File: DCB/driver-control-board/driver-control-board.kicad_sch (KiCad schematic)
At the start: 34 parts, among them U1 STM32F413CGUx, U2 LD1117S33TR_SOT223

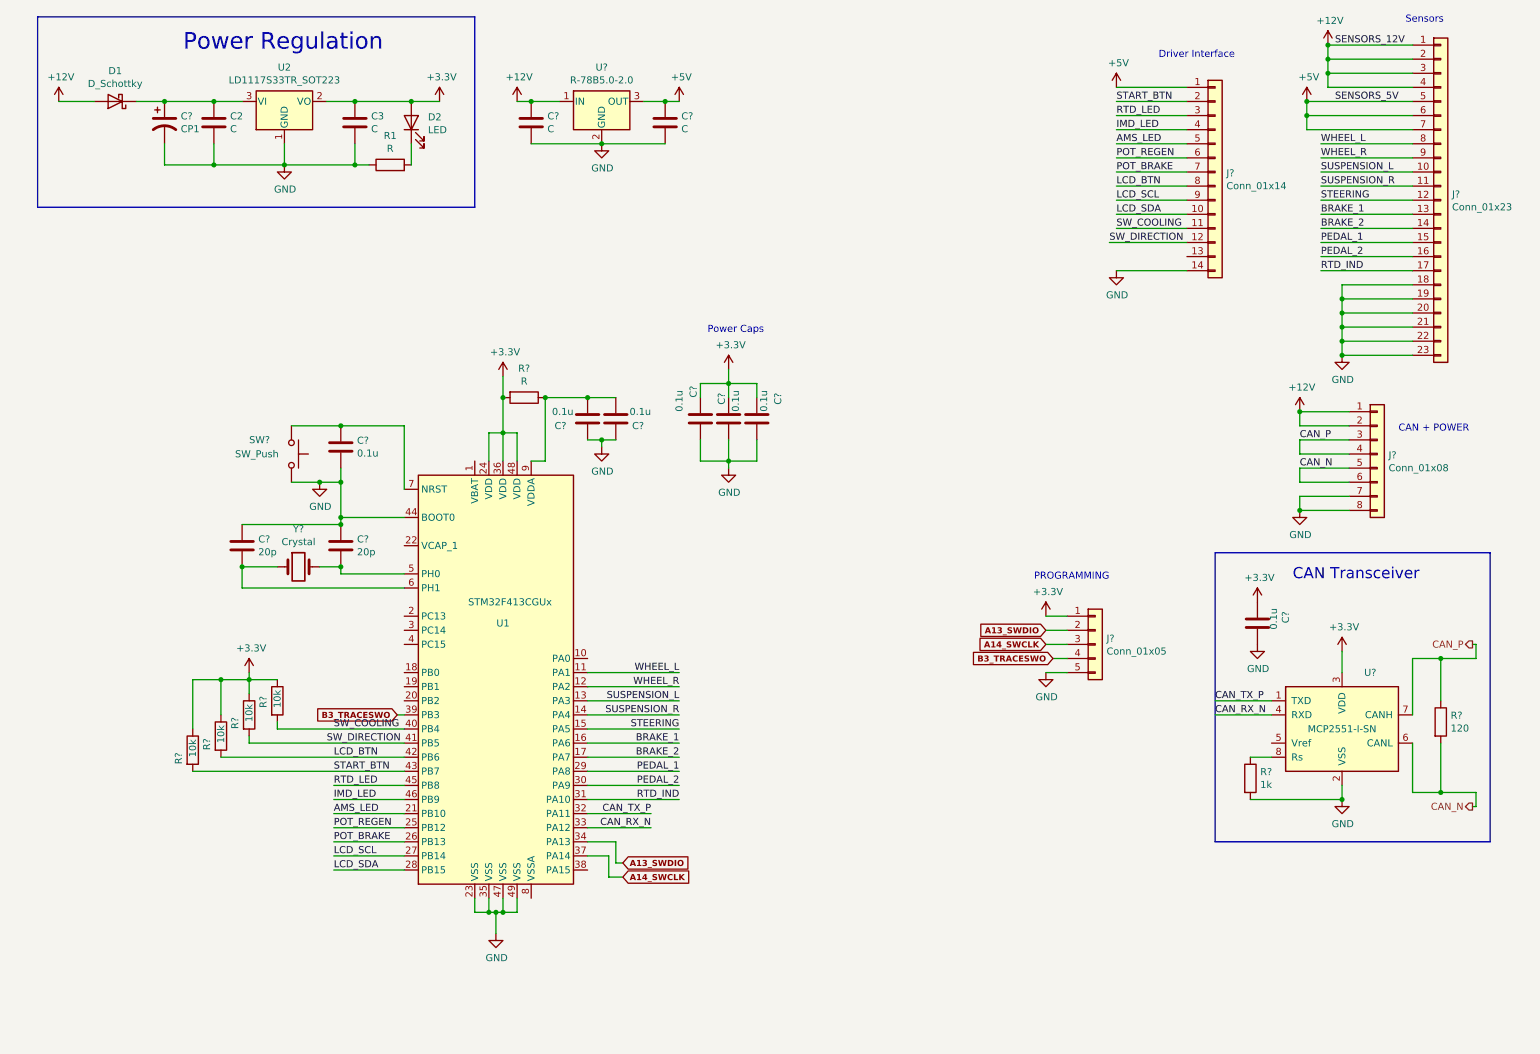
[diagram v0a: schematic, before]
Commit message: DCB Layout Rev 1 Complete
Complete the layout first draft
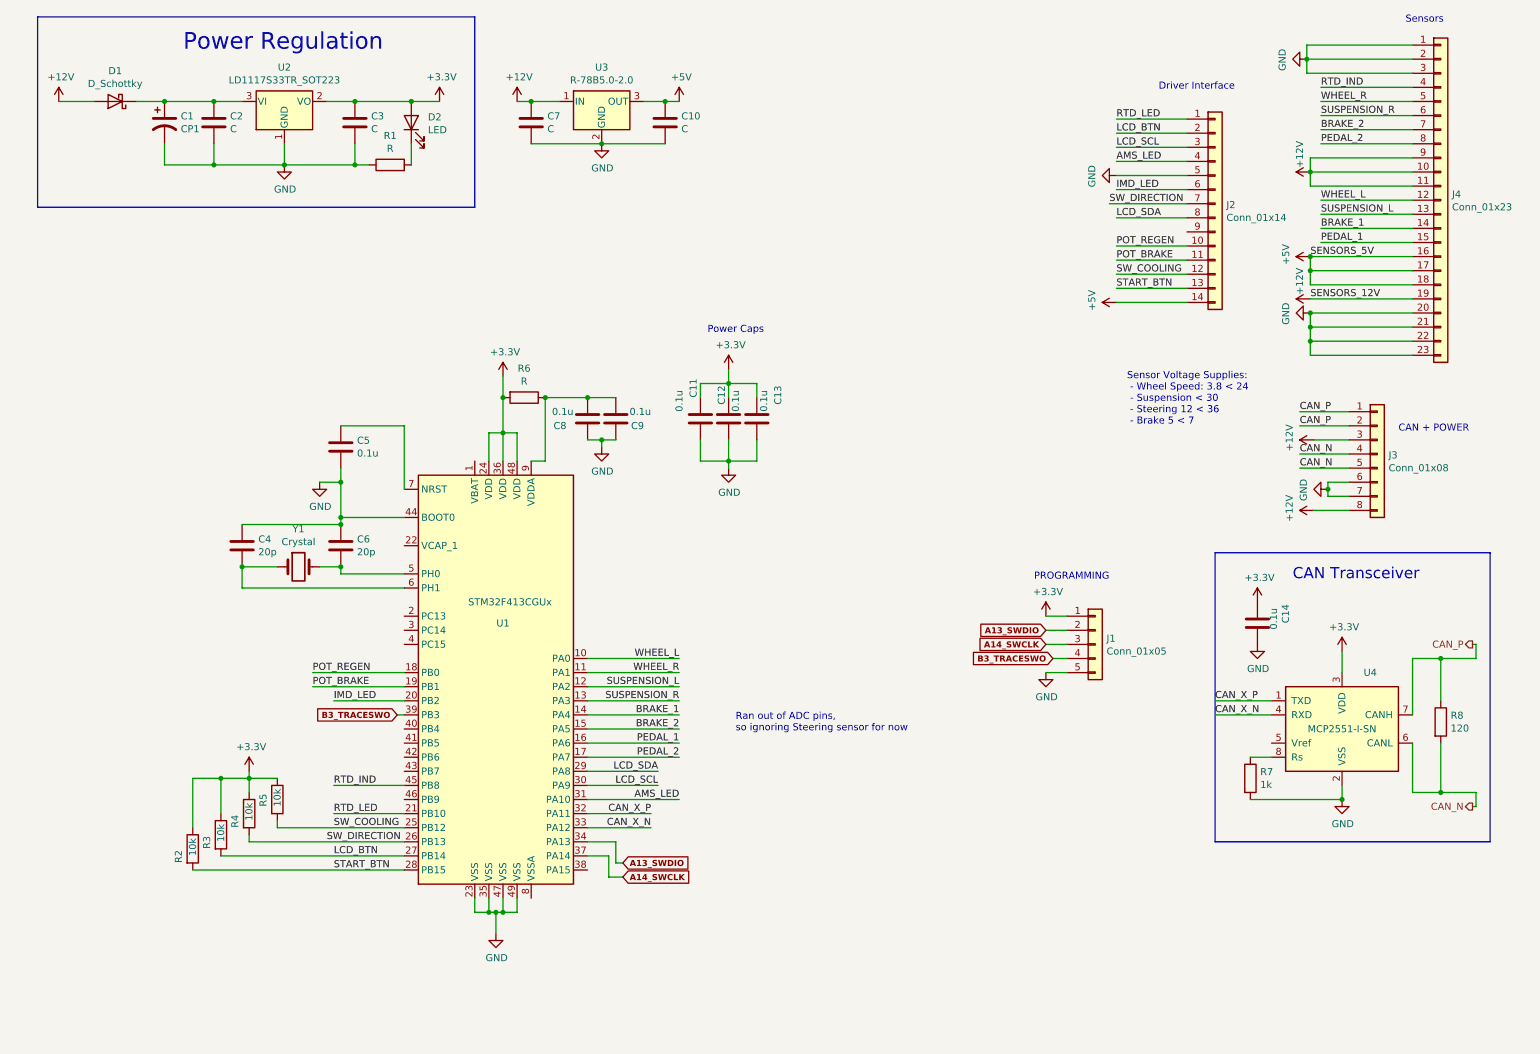
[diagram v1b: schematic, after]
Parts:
- removed SW?: SW_Push, symbol Switch:SW_Push
- C1: renamed from C?; footprint (none) -> Capacitor_THT:CP_Radial_D4.0mm_P2.00mm
- C10, C11, C12, C13, C14, C4, C5, C6, C7, C8, C9: renamed from C?; footprint (none) -> Capacitor_SMD:C_0603_1608Metric_Pad1.08x0.95mm_HandSolder
- C2, C3: footprint (none) -> Capacitor_SMD:C_0603_1608Metric_Pad1.08x0.95mm_HandSolder
- D1: footprint (none) -> Diode_SMD:D_SMA-SMB_Universal_Handsoldering
- D2: footprint (none) -> LED_SMD:LED_0603_1608Metric_Pad1.05x0.95mm_HandSolder
- J1: renamed from J?; footprint (none) -> Connector_JST:JST_XH_B5B-XH-A_1x05_P2.50mm_Vertical
- J2: renamed from J?; footprint (none) -> AERO_Footprints:TE_1-776266-1_14pin_Horizontal
- J3: renamed from J?; footprint (none) -> AERO_Footprints:TE_1-776280-1_8pin_Horizontal
- J4: renamed from J?; footprint (none) -> AERO_Footprints:TE_1-770669-1_23pin_Horizontal
- R1: footprint (none) -> Resistor_SMD:R_0603_1608Metric_Pad0.98x0.95mm_HandSolder
- R2, R3, R4, R5, R6, R7, R8: renamed from R?; footprint (none) -> Resistor_SMD:R_0603_1608Metric_Pad0.98x0.95mm_HandSolder
- Y1: renamed from Y?; footprint (none) -> Crystal:Crystal_HC52-8mm_Vertical
- gave numbers to parts that had none: 2
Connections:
- net +12V: now also J3.3 (Pin_3), J3.8 (Pin_8), J4.10 (Pin_10), J4.11 (Pin_11), J4.19 (Pin_19), J4.9 (Pin_9); no longer J3.1 (Pin_1), J3.2 (Pin_2), J4.1 (Pin_1), J4.2 (Pin_2), J4.3 (Pin_3), J4.4 (Pin_4)
- net +5V: now also J2.14 (Pin_14), J4.16 (Pin_16), J4.17 (Pin_17), J4.18 (Pin_18); no longer J2.1 (Pin_1), J4.5 (Pin_5), J4.6 (Pin_6), J4.7 (Pin_7)
- net AMS_LED: now also J2.4 (Pin_4), U1.31 (PA10); no longer J2.5 (Pin_5), U1.21 (PB10)
- net BRAKE_1: now also J4.14 (Pin_14), U1.14 (PA4); no longer J4.13 (Pin_13), U1.16 (PA6)
- net BRAKE_2: now also J4.7 (Pin_7), U1.15 (PA5); no longer J4.14 (Pin_14), U1.17 (PA7)
- net CAN_N: now also J3.4 (Pin_4); no longer J3.6 (Pin_6)
- net CAN_P: now also J3.1 (Pin_1), J3.2 (Pin_2); no longer J3.3 (Pin_3), J3.4 (Pin_4)
- net GND: now also J2.5 (Pin_5), J3.6 (Pin_6), J4.1 (Pin_1), J4.2 (Pin_2), J4.3 (Pin_3); no longer J2.14 (Pin_14), J3.8 (Pin_8), J4.18 (Pin_18), J4.19 (Pin_19)
- net IMD_LED: now also J2.6 (Pin_6), U1.20 (PB2); no longer J2.4 (Pin_4), U1.46 (PB9)
- net LCD_BTN: now also J2.2 (Pin_2), U1.27 (PB14); no longer J2.8 (Pin_8), U1.42 (PB6)
- net LCD_SCL: now also J2.3 (Pin_3), U1.30 (PA9); no longer J2.9 (Pin_9), U1.27 (PB14)
- net LCD_SDA: now also J2.8 (Pin_8), U1.29 (PA8); no longer J2.10 (Pin_10), U1.28 (PB15)
- net PEDAL_1: now also U1.16 (PA6); no longer U1.29 (PA8)
- net PEDAL_2: now also J4.8 (Pin_8), U1.17 (PA7); no longer J4.16 (Pin_16), U1.30 (PA9)
- net POT_BRAKE: now also J2.11 (Pin_11), U1.19 (PB1); no longer J2.7 (Pin_7), U1.26 (PB13)
- net POT_REGEN: now also J2.10 (Pin_10), U1.18 (PB0); no longer J2.6 (Pin_6), U1.25 (PB12)
- net RTD_IND: now also J4.4 (Pin_4), U1.45 (PB8); no longer J4.17 (Pin_17), U1.31 (PA10)
- net RTD_LED: now also J2.1 (Pin_1), U1.21 (PB10); no longer J2.3 (Pin_3), U1.45 (PB8)
- net START_BTN: now also J2.13 (Pin_13), U1.28 (PB15); no longer J2.2 (Pin_2), U1.43 (PB7)
- net SUSPENSION_L: now also J4.13 (Pin_13), U1.12 (PA2); no longer J4.10 (Pin_10), U1.13 (PA3)
- net SUSPENSION_R: now also J4.6 (Pin_6), U1.13 (PA3); no longer J4.11 (Pin_11), U1.14 (PA4)
- net SW_COOLING: now also J2.12 (Pin_12), U1.25 (PB12); no longer J2.11 (Pin_11), U1.40 (PB4)
- net SW_DIRECTION: now also J2.7 (Pin_7), U1.26 (PB13); no longer J2.12 (Pin_12), U1.41 (PB5)
- net WHEEL_L: now also J4.12 (Pin_12), U1.10 (PA0); no longer J4.8 (Pin_8), U1.11 (PA1)
- net WHEEL_R: now also J4.5 (Pin_5), U1.11 (PA1); no longer J4.9 (Pin_9), U1.12 (PA2)
- net CAN_RX_N renamed CAN_X_N
- net CAN_TX_P renamed CAN_X_P
- removed net STEERING: J4.12 (Pin_12), U1.15 (PA5)
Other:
- note added: "Ran out of ADC pins, so ignoring Steering sensor for now"
- note added: "Sensor Voltage Supplies: - Wheel Speed: 3.8 < 24 - Suspension < 30 - Steering 12 < 36 - Brake 5 < 7"
- moved on the sheet: J2, R2, R3, R4, R5

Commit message: adding mounting holes
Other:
- note added: "Ran out of ADC pins, so ignoring Steering sensor for now In the future, use another ADC chip and communicate over I2C"
- note removed: "Ran out of ADC pins, so ignoring Steering sensor for now"
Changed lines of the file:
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@@
     (effects (font (size 1.27 1.27)) (justify left bottom))
   )
-  (text "Ran out of ADC pins, \nso ignoring Steering sensor for now"
-    (at 143.51 142.875 0)
+  (text "Ran out of ADC pins, \nso ignoring Steering sensor for now\nIn the future, use another ADC chip\nand communicate over I2C\n"
+    (at 142.875 144.78 0)
     (effects (font (size 1.27 1.27)) (justify left bottom))
   )

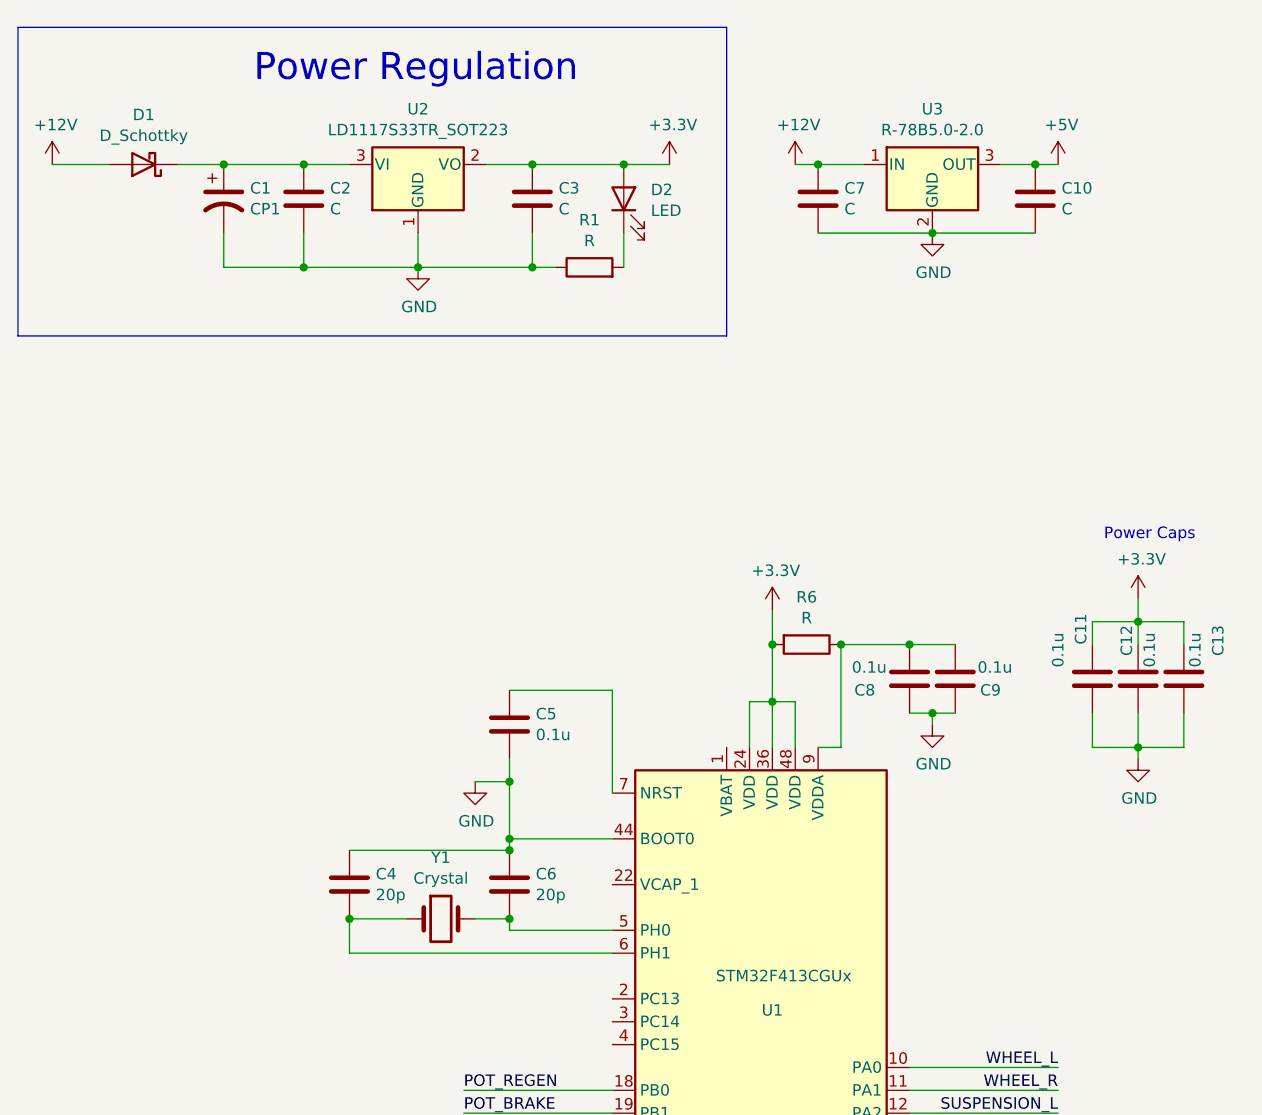
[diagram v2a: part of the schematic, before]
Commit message: updating filtering cap layout
Kay suggested layout changes. Moved caps around
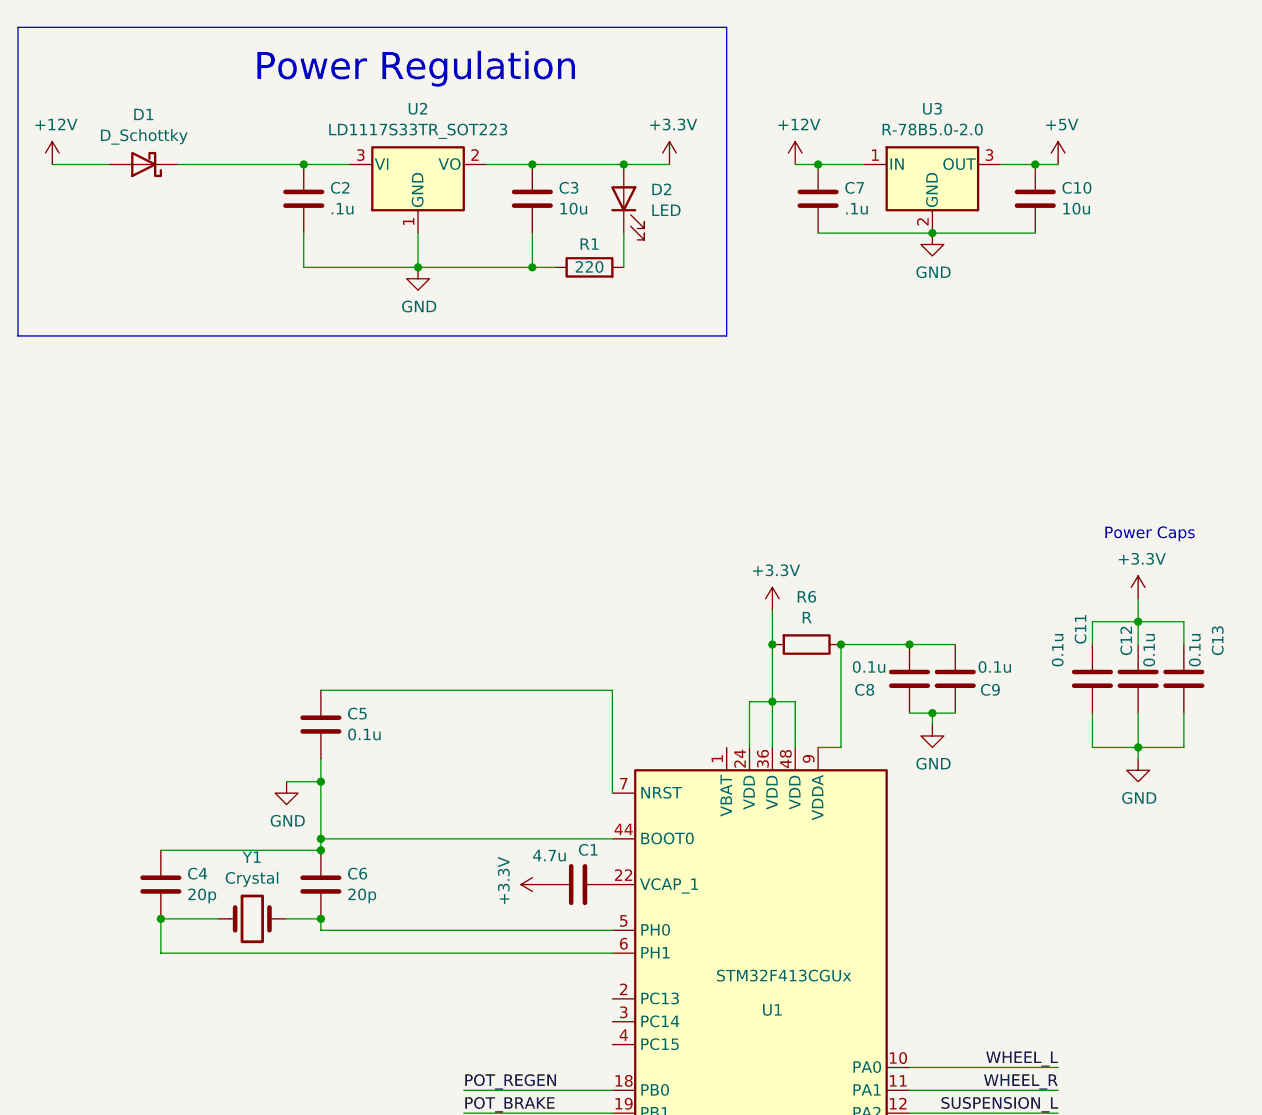
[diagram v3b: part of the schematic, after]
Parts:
- removed C1: CP1, Capacitor_THT:CP_Radial_D4.0mm_P2.00mm, symbol Device:CP1
- added C1: 4.7u, Capacitor_SMD:C_0603_1608Metric_Pad1.08x0.95mm_HandSolder, symbol Device:C
- C10, C3: value C -> 10u
- C2, C7: value C -> .1u
- R1: value R -> 220
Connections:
- net +3V3: now also C1.2
- net at U1.22 (VCAP_1): now also C1.1
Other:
- moved on the sheet: C4, C5, C6, Y1

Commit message: working on layout
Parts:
- removed R2, R3, R4, R5: 10k, Resistor_SMD:R_0603_1608Metric_Pad0.98x0.95mm_HandSolder, symbol Device:R
- added J5: Conn_02x10_Counter_Clockwise, Connector_PinHeader_2.54mm:PinHeader_2x10_P2.54mm_Horizontal, symbol Connector_Generic:Conn_02x10_Counter_Clockwise
- added J6: Conn_01x14, AERO_Footprints:TE_1-776266-1_14pin_Horizontal, symbol Connector_Generic:Conn_01x14
- added RN1: R_Pack04, Resistor_SMD:R_Array_Convex_4x1206, symbol Device:R_Pack04
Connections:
- net +12V: now also J3.1 (Pin_1), J3.6 (Pin_6), J5.1 (Pin_1); no longer J3.3 (Pin_3), J3.8 (Pin_8)
- net +3V3: now also RN1.5 (R4.2), RN1.6 (R3.2), RN1.7 (R2.2), RN1.8 (R1.2)
- net CAN_N: now also J3.2 (Pin_2), J5.3 (Pin_3); no longer J3.5 (Pin_5)
- net CAN_P: now also J3.3 (Pin_3), J3.5 (Pin_5), J5.5 (Pin_5); no longer J3.1 (Pin_1), J3.2 (Pin_2)
- net GND: now also J3.8 (Pin_8), J5.2 (Pin_2), J6.10 (Pin_10); no longer J3.6 (Pin_6)
- net LCD_BTN: now also RN1.2 (R2.1)
- net START_BTN: now also RN1.1 (R1.1)
- net SW_COOLING: now also RN1.4 (R4.1)
- net SW_DIRECTION: now also RN1.3 (R3.1)
- new net 12V_OUT: J5.4 (Pin_4), J6.11 (Pin_11)
- new net 5V_OUT: J5.6 (Pin_6), J6.12 (Pin_12)
- new net BUZZER: J5.15 (Pin_15)
- new net CURRENT_1: J5.17 (Pin_17), J6.4 (Pin_4)
- new net CURRENT_2: J5.18 (Pin_18), J6.9 (Pin_9)
- new net CURRENT_3: J5.19 (Pin_19), J6.5 (Pin_5)
- new net CURRENT_GND: J5.16 (Pin_16), J6.14 (Pin_14)
- new net DISP+: J5.7 (Pin_7), J6.1 (Pin_1)
- new net DISP-: J5.9 (Pin_9), J6.6 (Pin_6)
- new net FAN: J5.10 (Pin_10)
- new net Heater: J5.8 (Pin_8), J6.13 (Pin_13)
- new net USB_D+: J5.11 (Pin_11), J6.2 (Pin_2)
- new net USB_D-: J5.13 (Pin_13), J6.7 (Pin_7)
- new net USB_GND: J5.12 (Pin_12), J6.3 (Pin_3)
- new net USB_PWR: J5.14 (Pin_14), J6.8 (Pin_8)
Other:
- note added: "Ampseal output"
- note added: "Passthrough to BMS Module"
- note added: "RX"
- note added: "TX"
- moved on the sheet: C1, C10, C11, C12, C13, C14, C4, C5, C6, C7, C8, C9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
